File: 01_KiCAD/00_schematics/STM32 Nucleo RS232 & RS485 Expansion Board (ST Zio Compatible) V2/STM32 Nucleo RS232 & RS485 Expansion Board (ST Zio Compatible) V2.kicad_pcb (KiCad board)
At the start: 4 copper layers, 70 x 133.4 mm, 176 parts, among them CN10 Conn_02x17_Odd_Even, CN7 Conn_02x10_Odd_Even, CN8 Conn_02x08_Odd_Even, CN9 Conn_02x15_Odd_Even, IC1 REG103GA-A, J1 1190299, J10 DIR, J11 TERM_TX, J12 TERM_RX, J13 SLR, J2 CONN D-SUB PLUG 9POS TH, J3 TCVR_PWR, J4 TX_LED, J5 RX_LED, J6 SW_ENA, J7 MODE0, J8 MODE1, J9 MODE2, Q1 BSS84, U1 TPS2117DRLR, U11 SN74LVC2G14DBV, U12 SN74LVC14ADR, U2 THVD4431RHAR, U3 SN74LVC2G14DBV, U4 SN74LVC245ADBR, U5 SN74LVC14ADR

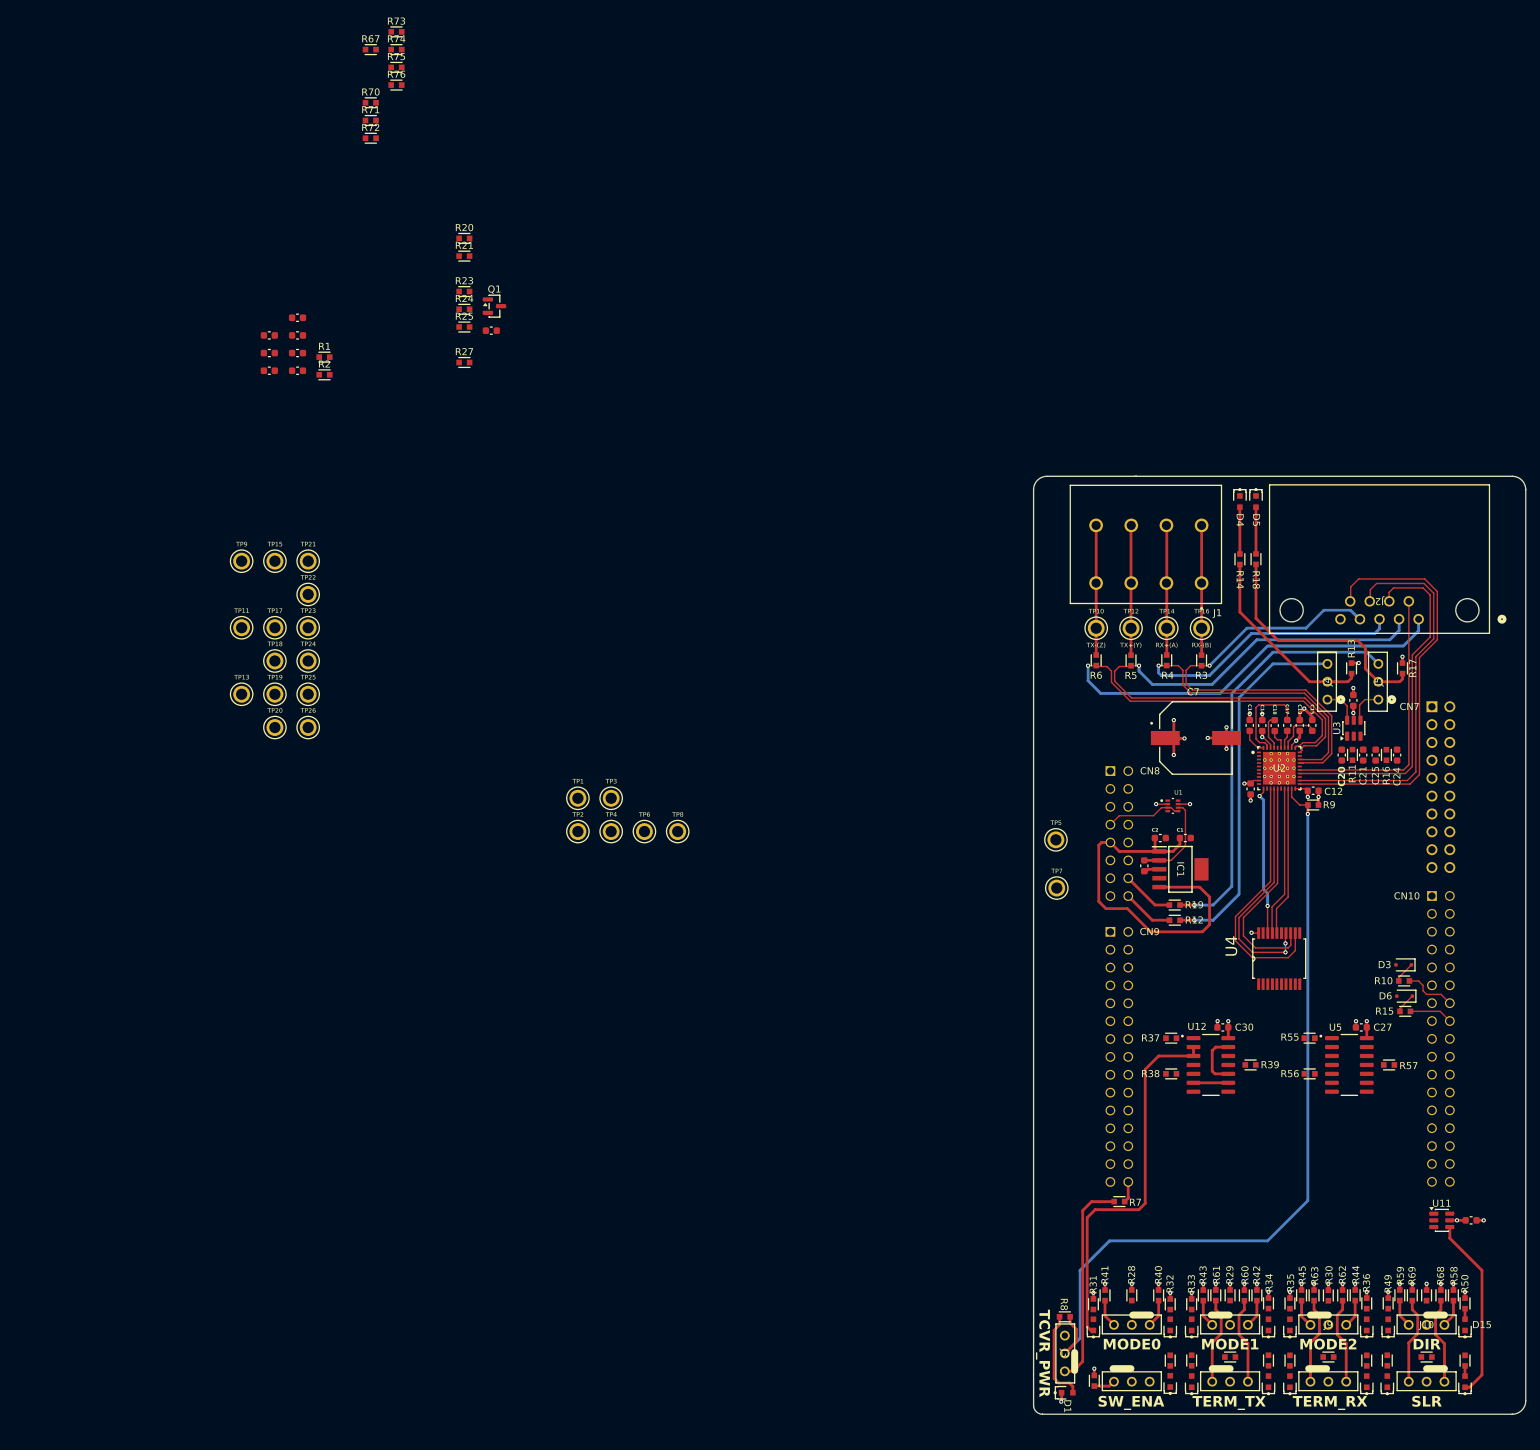
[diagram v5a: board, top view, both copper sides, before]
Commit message: Added half-duplex jumpers
Addres jumpers for hardware RS485 half-duplex configuration combining signals A(Y) & B(Z). Finalising testpoints and added 3D models for each test-point color.
-Green = logic side
-Blue = connector side
Made some minor changed to layout for test signals clarification (THVD4431 sheet)
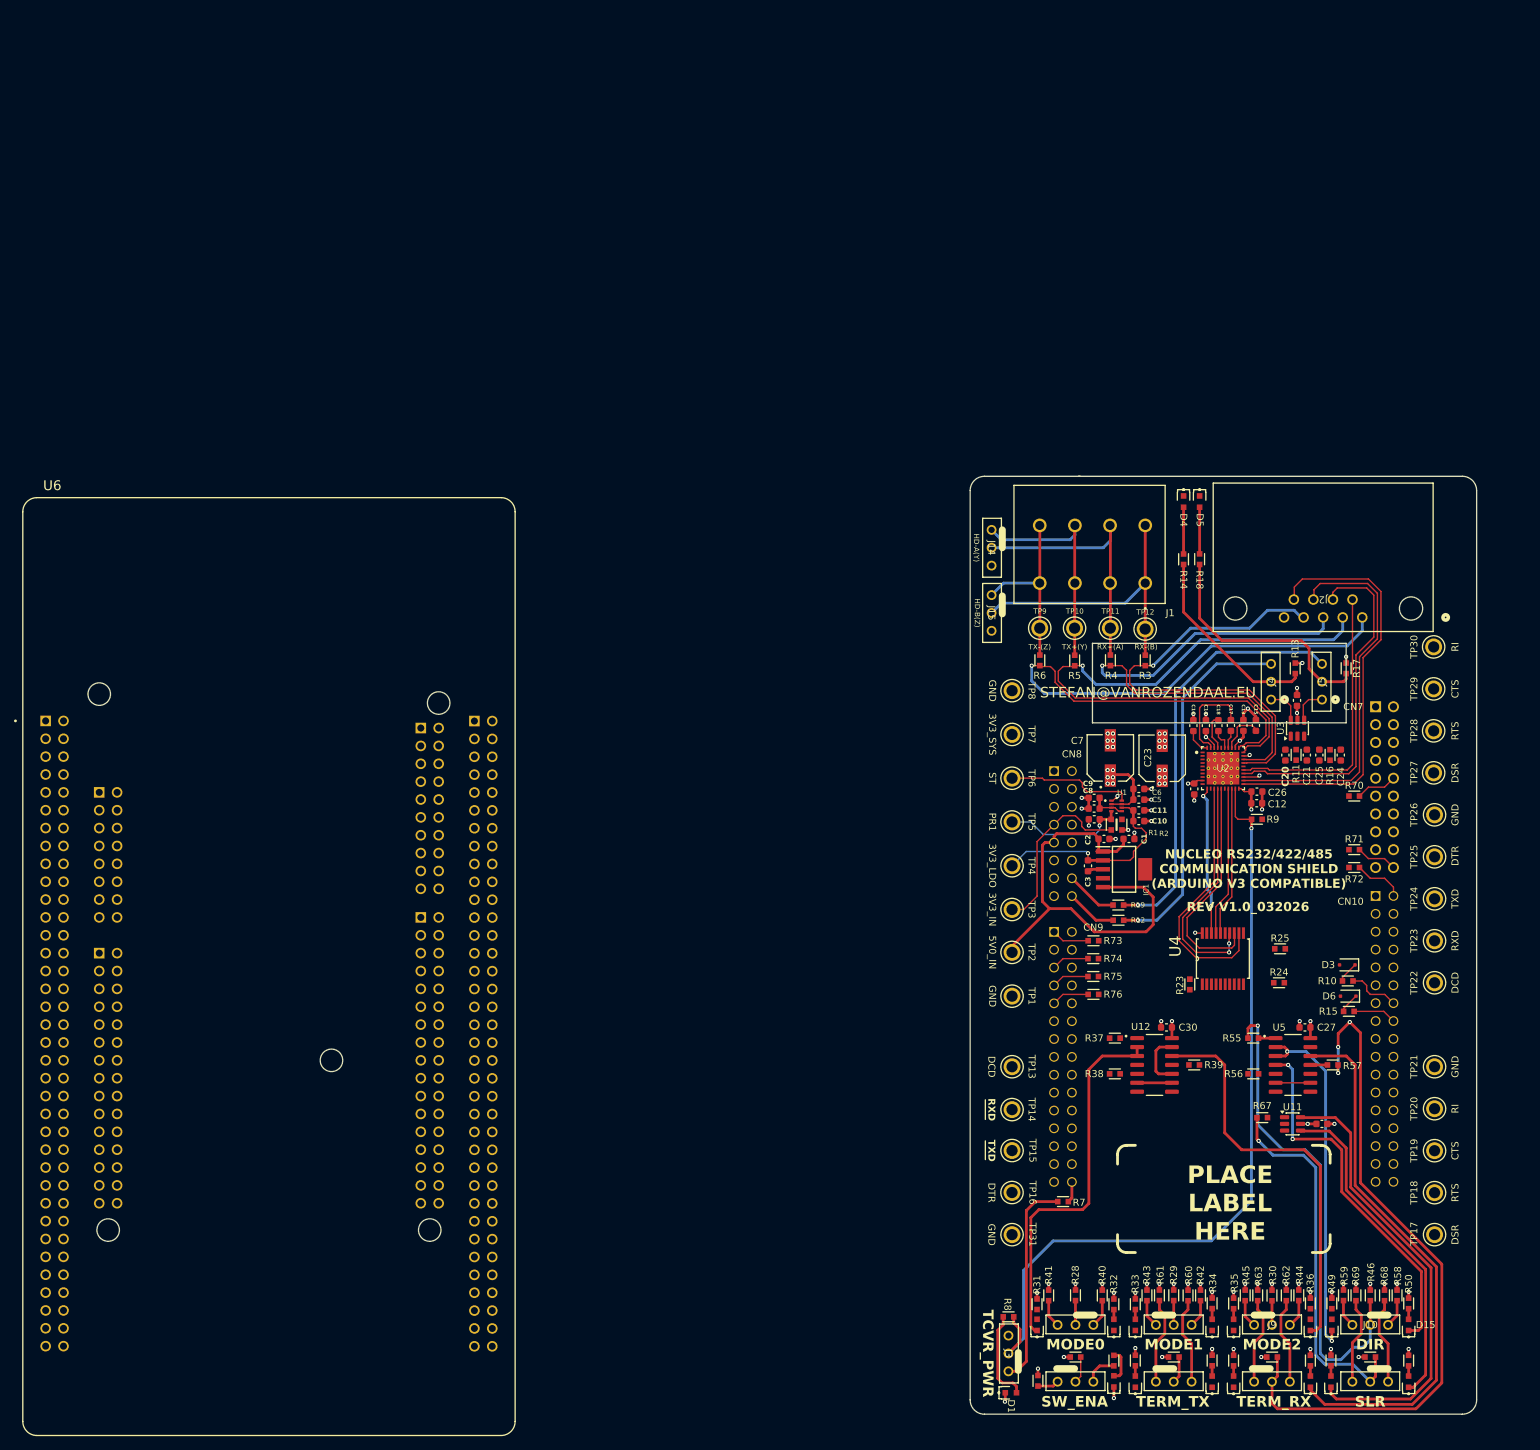
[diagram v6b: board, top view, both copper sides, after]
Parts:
- removed Q1: BSS84, Package_TO_SOT_SMD:SOT-23
- removed R20: 1K, PCM_fab:R_0603
- removed R21: 10K, PCM_fab:R_0603
- added C23: 47µF, EEEFT1H470AP:CAP_EEEFT1H470AP, F.Cu at (55.1, 76.9)
- added J14: HD-A(Y), Samtec_Connector:Samtec HTSW-103-07-F-S, F.Cu at (30.9, 47.0)
- added J15: HD-B(Z), Samtec_Connector:Samtec HTSW-103-07-F-S, F.Cu at (30.9, 56.3)
- added TP27: DSR, 5008_Orange:KEYSTONE_5008, F.Cu at (93.7, 79.0)
- added TP28: RTS, 5008_Orange:KEYSTONE_5008, F.Cu at (93.7, 73.0)
- added TP29: CTS, 5008_Orange:KEYSTONE_5008, F.Cu at (93.7, 67.1)
- added TP30: RI, 5008_Orange:KEYSTONE_5008, F.Cu at (93.7, 61.1)
- added TP31: GND, 5006_Black:KEYSTONE_5006, F.Cu at (33.8, 144.7)
- added U6: NUCLEO-H753ZI, NUCLEO-H753ZI:MODULE_NUCLEO-H753ZI, F.Cu at (-71.9, 106.5)
- C7: footprint EEEHD1H101P:CAP_EEEHD1H101P -> EEEFT1H470AP:CAP_EEEFT1H470AP
- TP1: value 3V3_LDO -> GND; footprint 5005_Red:KEYSTONE_5005 -> 5006_Black:KEYSTONE_5006
- TP10: value TX-(Z) -> TX+(Y); footprint 5008_Orange:KEYSTONE_5008 -> 5009_Yellow:KEYSTONE_5009
- TP11: value L2-RXD -> RX+(A); footprint 5009_Yellow:KEYSTONE_5009 -> 5008_Orange:KEYSTONE_5008
- TP12: value TX+(Y) -> RX-(B)
- TP13: value L3-TXD -> DCD
- TP14: value RX+(A) -> RXD; footprint 5008_Orange:KEYSTONE_5008 -> 5009_Yellow:KEYSTONE_5009
- TP15: value L4-DTR -> TXD
- TP16: value RX-(B) -> DTR; footprint 5008_Orange:KEYSTONE_5008 -> 5009_Yellow:KEYSTONE_5009
- TP17: value L5-DSR -> DSR
- TP18: value R5-DSR -> RTS; footprint 5008_Orange:KEYSTONE_5008 -> 5009_Yellow:KEYSTONE_5009
- TP19: value L6-RTS -> CTS
- TP2: value 5006 -> 5V0_IN; footprint 5006_Black:KEYSTONE_5006 -> 5005_Red:KEYSTONE_5005
- TP20: value R6-RTS -> RI; footprint 5008_Orange:KEYSTONE_5008 -> 5009_Yellow:KEYSTONE_5009
- TP21: value L7-CTS -> GND; footprint 5009_Yellow:KEYSTONE_5009 -> 5006_Black:KEYSTONE_5006
- TP22: value R7-CTS -> DCD; footprint 5008_Orange:KEYSTONE_5008 -> 5009_Yellow:KEYSTONE_5009
- TP23: value L8-RI -> RXD
- TP24: value 5008 -> TXD
- TP25: value GND -> DTR; footprint 5006_Black:KEYSTONE_5006 -> 5008_Orange:KEYSTONE_5008
- TP3: value 5006 -> 3V3_IN; footprint 5006_Black:KEYSTONE_5006 -> 5005_Red:KEYSTONE_5005
- TP4: value PR1 -> 3V3_LDO
- TP5: value 3V0 -> PR1
- TP6: value 3V3_SYS -> ST; footprint 5005_Red:KEYSTONE_5005 -> 5007_White:KEYSTONE_5007
- TP7: value 5V0 -> 3V3_SYS
- TP8: value ST -> GND; footprint 5007_White:KEYSTONE_5007 -> 5006_Black:KEYSTONE_5006
- TP9: value L1-DCD -> TX-(Z)
- moved R67 197.8 mm to (69.3, 128.0)
- moved TP17 186.1 mm to (93.8, 144.7)
- moved TP18 181.4 mm to (93.8, 138.7)
- moved TP19 177.2 mm to (93.8, 132.7)
- moved TP21 175.5 mm to (93.8, 120.8)
- moved R72 174.1 mm to (82.4, 92.5)
- moved R71 174.1 mm to (82.4, 89.9)
- moved TP20 173.6 mm to (93.8, 126.7)
- moved R70 171.1 mm to (82.4, 82.3)
- moved TP22 169.4 mm to (93.8, 108.8)
- moved TP23 166.2 mm to (93.8, 102.9)
- moved R27 166.0 mm to (42.8, 162.1), turned to 180 degrees
- moved TP24 163.7 mm to (93.8, 96.9)
- moved R76 162.9 mm to (45.3, 110.5), turned to 180 degrees
- moved R75 162.9 mm to (45.3, 108.0)
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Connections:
- TP1 pad TP: 3V3_LDO -> GND
- TP10 pad TP: /RS232 & RS485 Tranceiver/TX- (Z) -> /RS232 & RS485 Tranceiver/TX+ (Y)
- TP11 pad TP: L2-RXD -> /RS232 & RS485 Tranceiver/RX+ (A)
- TP12 pad TP: /RS232 & RS485 Tranceiver/TX+ (Y) -> /RS232 & RS485 Tranceiver/RX- (B)
- TP13 pad TP: L3-TXD -> L1-DCD
- TP14 pad TP: /RS232 & RS485 Tranceiver/RX+ (A) -> L2-RXD
- TP15 pad TP: L4-DTR -> L3-TXD
- TP16 pad TP: /RS232 & RS485 Tranceiver/RX- (B) -> L4-DTR
- TP18 pad TP: unconnected-(TP18-PadTP) -> L6-RTS
- TP19 pad TP: L6-RTS -> L7-CTS
- TP2 pad TP: GND -> ARDUINO_5V
- TP20 pad TP: unconnected-(TP20-PadTP) -> L8-RI
- TP21 pad TP: L7-CTS -> GND
- TP22 pad TP: unconnected-(TP22-PadTP) -> /RS232 & RS485 Tranceiver/TX-
- TP23 pad TP: L8-RI -> /RS232 & RS485 Tranceiver/TX+
- TP24 pad TP: unconnected-(TP24-PadTP) -> /RS232 & RS485 Tranceiver/RX+
- TP25 pad TP: GND -> /RS232 & RS485 Tranceiver/RX-
- TP3 pad TP: GND -> NUCLEO_3V3
- TP4 pad TP: Net-(U1-PR1) -> 3V3_LDO
- TP5 pad TP: NUCLEO_3V3 -> Net-(U1-PR1)
- TP6 pad TP: 3V3_SYS -> Net-(U1-ST)
- TP7 pad TP: ARDUINO_5V -> 3V3_SYS
- TP8 pad TP: Net-(U1-ST) -> GND
- TP9 pad TP: L1-DCD -> /RS232 & RS485 Tranceiver/TX- (Z)
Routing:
- net TERM_RX: track 21.6 -> 120.3 mm, vias 0 -> 3
- net Net-(D19-K): track 0.00 -> 77.1 mm
- net DIR: track 0.00 -> 69.3 mm, vias 0 -> 1
- net Net-(D20-K): track 0.00 -> 64.4 mm
- net Net-(D13-K): track 0.00 -> 57.7 mm
- net SLR: track 21.3 -> 74.1 mm, vias 2 -> 3
- net Net-(D15-K): track 0.00 -> 52.2 mm, vias 0 -> 2
- net Net-(D14-K): track 0.00 -> 51.0 mm, vias 0 -> 2
- net /RS232 & RS485 Tranceiver/RX- (B): track 18.4 -> 42.0 mm
- net Net-(D21-K): track 26.1 -> 47.6 mm
- net /RS232 & RS485 Tranceiver/RX+ (A): track 18.4 -> 37.9 mm
- net NUCLEO_3V3: track 10.8 -> 30.3 mm
- net Net-(U1-ST): track 0.00 -> 17.9 mm
- net Net-(U1-PR1): track 0.00 -> 17.8 mm, vias 0 -> 1
- net 3V3_LDO: track 13.8 -> 30.5 mm, vias 0 -> 1
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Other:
- board size 70 x 133.4 mm -> 72 x 133.4 mm
- board text added: "NUCLEO RS232/422/485 COMMUNICATION SHIELD (ARDUINO V3 COMPATIBLE)"
- board text added: "PLACE LABEL HERE"
- board text added: "REV V1.0_032026"
- board text added: "STEFAN@VANROZENDAAL.EU"
